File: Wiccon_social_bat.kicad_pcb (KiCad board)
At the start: 2 copper layers, 84.5 x 43.3 mm, 19 parts, among them J1 SAO, SW1 Change, U1 CH32V003

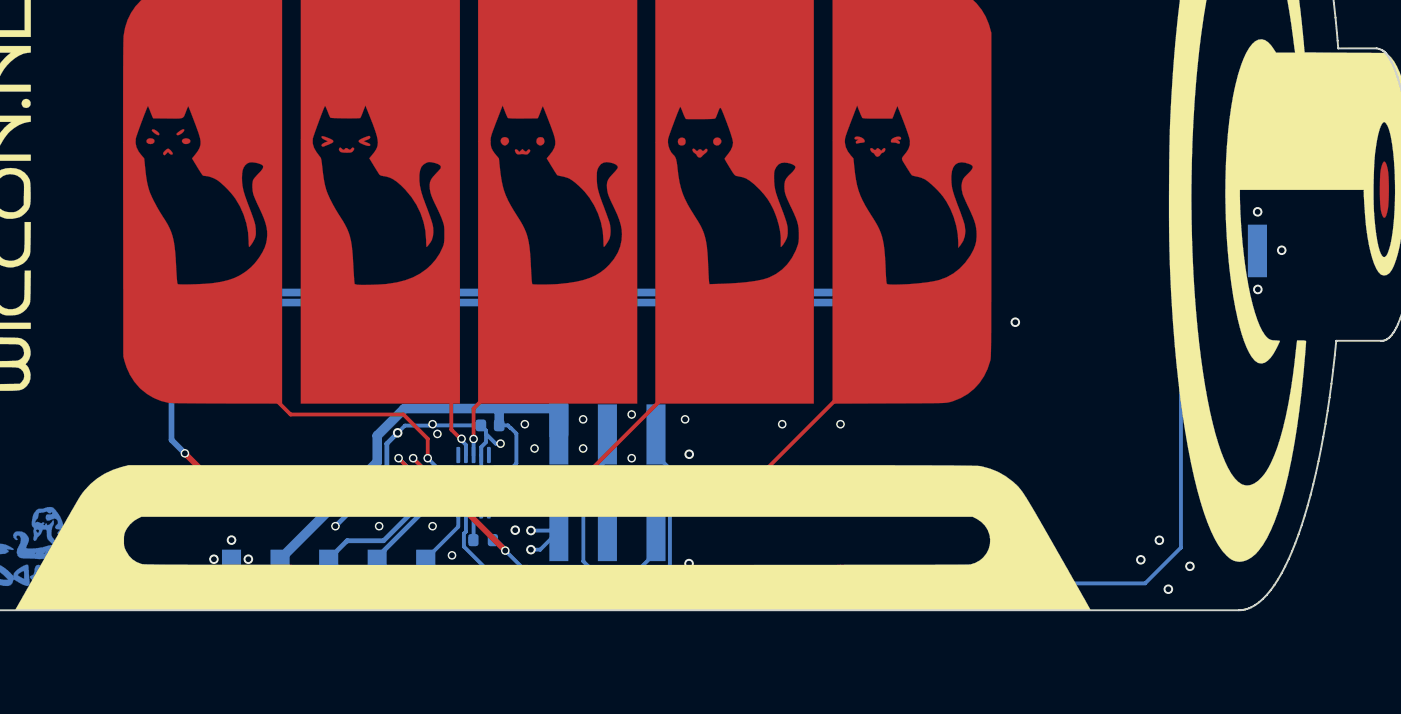
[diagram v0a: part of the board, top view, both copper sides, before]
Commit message: Small changes to art, changed sw1
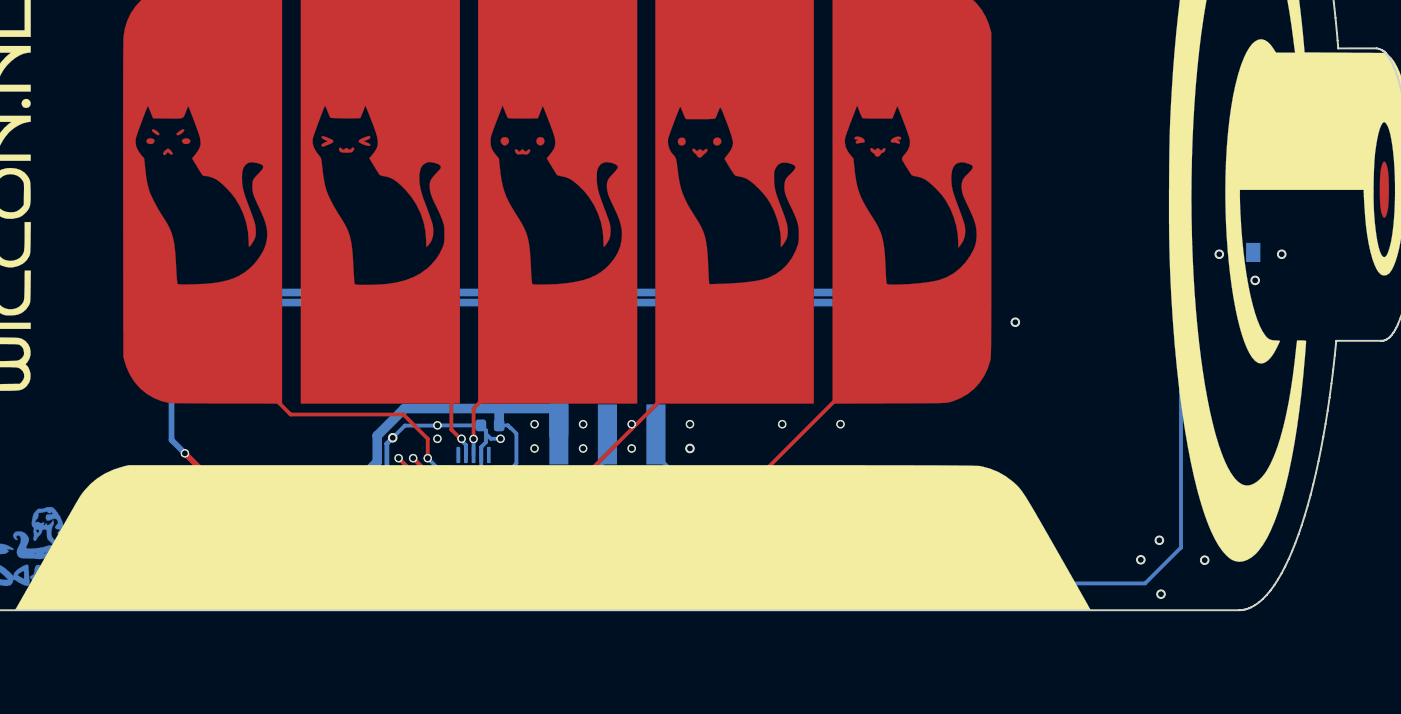
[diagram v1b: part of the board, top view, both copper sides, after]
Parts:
- SW1: footprint Button_Switch_SMD:SW_SPST_B3SL-1002P -> Button_Switch_SMD:SW_Push_1P1T_XKB_TS-1187A
- moved SW1 0.10 mm to (31.9, -0.05)

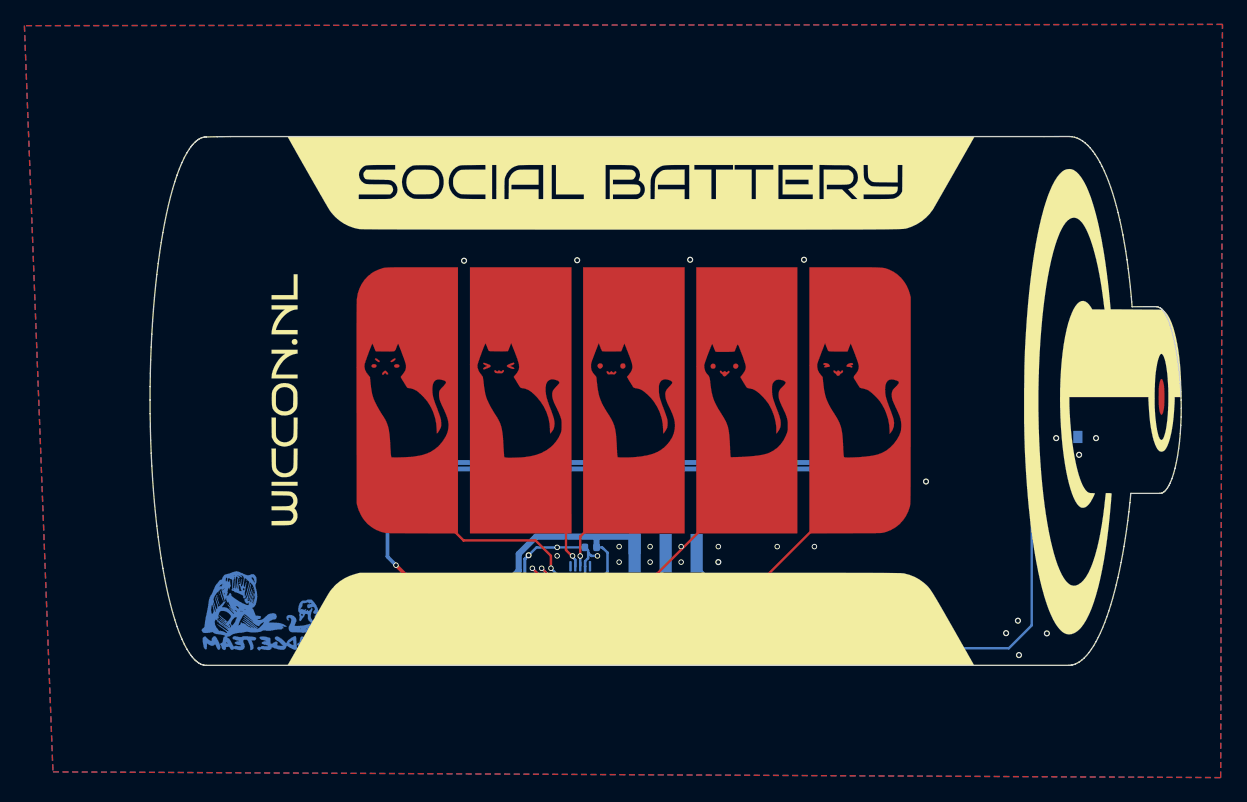
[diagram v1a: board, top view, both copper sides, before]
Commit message: Move WICCON.NL text
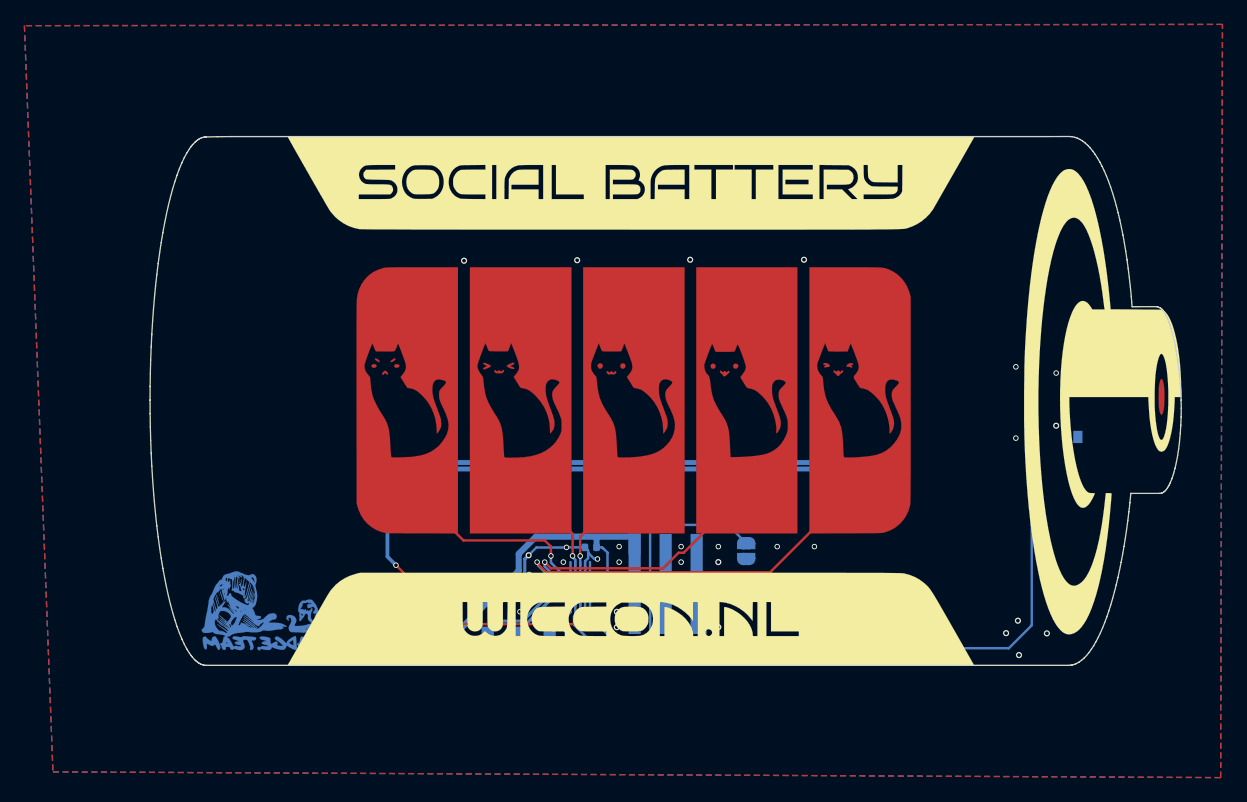
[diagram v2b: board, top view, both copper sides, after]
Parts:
- added JP1: Mode, Jumper:SolderJumper-2_P1.3mm_Open_RoundedPad1.0x1.5mm, B.Cu at (6.60, 12.3)
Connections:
- U1 pad 7: unconnected-(U1-PC0-Pad7) -> Net-(JP1-B)
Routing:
- net Net-(JP1-B): track 0.00 -> 16.8 mm
- net TOUCH5: track 28.9 -> 28.1 mm
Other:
- board text added: "A"
